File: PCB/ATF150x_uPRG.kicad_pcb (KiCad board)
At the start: 2 copper layers, 38.1 x 22.9 mm, 22 parts, among them J1 Adafruit_2264, J2 Altera JTAG-A+VPP, U2 MAX662A

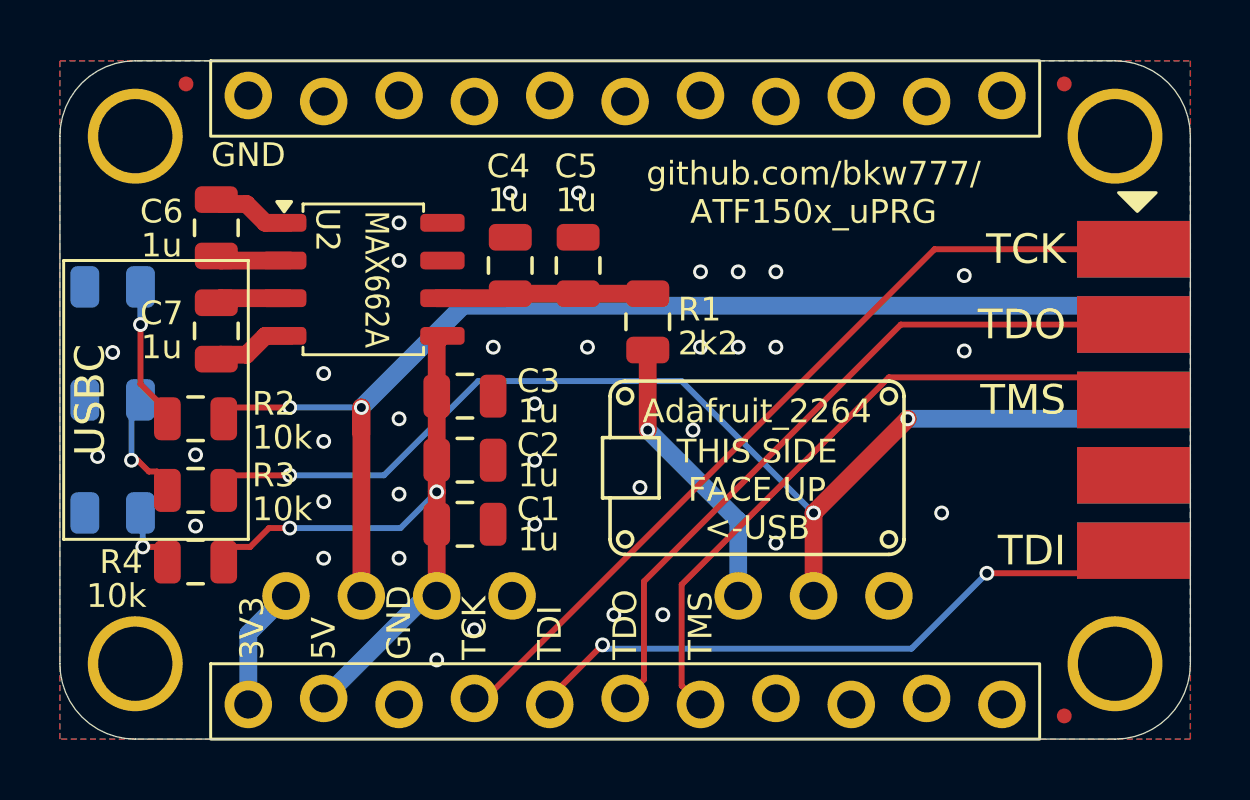
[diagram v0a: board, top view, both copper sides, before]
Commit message: adafruit board use max662 shutdown pin
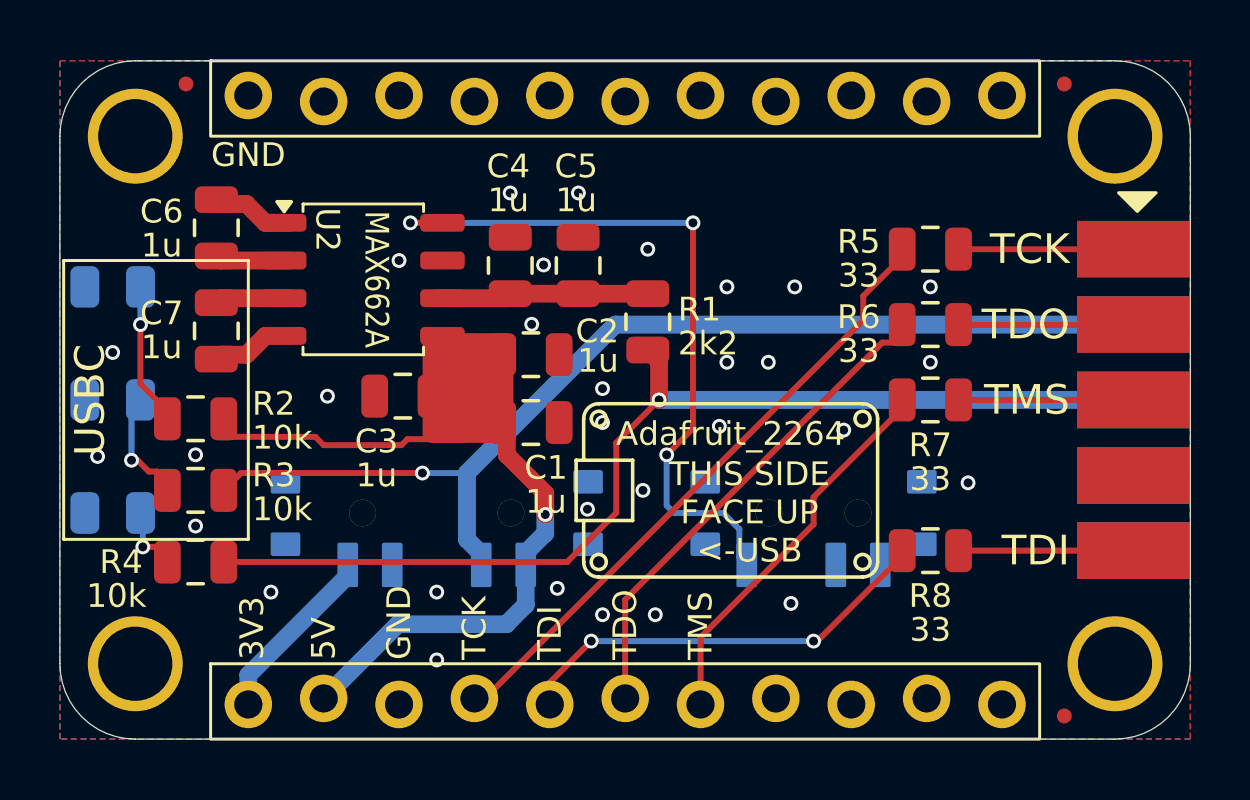
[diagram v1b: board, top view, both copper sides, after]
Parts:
- removed JP1: VCC, 000_LOCAL:PinHeader_1x04_P2.54mm_Horizontal
- removed JP2: VPP, 000_LOCAL:PinHeader_1x03_P2.54mm_Horizontal
- added R5: 33, 000_LOCAL:R_0805, F.Cu at (156.3, 90.2)
- added R6: 33, 000_LOCAL:R_0805, F.Cu at (156.3, 92.7)
- added R7: 33, 000_LOCAL:R_0805, F.Cu at (156.3, 95.2)
- added R8: 33, 000_LOCAL:R_0805, F.Cu at (156.3, 100.3)
- added SW1: VCC, 000_LOCAL:CUS-13B pth, B.Cu at (139.7, 99.1)
- added SW2: VPP, 000_LOCAL:CUS-12B pth, B.Cu at (152.4, 99.1)
- LED1: value VCC -> PWR
- LED2: value VPP -> VCC
- LED3: value PWR -> VPP
- moved C2 4.19 mm to (142.9, 93.7)
- moved C1 4.09 mm to (142.9, 96.0)
- moved C3 2.09 mm to (138.6, 95.1), turned to 180 degrees
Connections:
- J1 pad 4: TCK -> /TCK
- J1 pad 5: TDI -> /TDI
- J1 pad 6: TDO -> /TDO
- J1 pad 7: TMS -> /TMS
- J2 pad 1: TCK -> Net-(J2-TCK)
- J2 pad 3: TDO -> Net-(J2-TDO)
- J2 pad 5: TMS -> Net-(J2-TMS)
- J2 pad 9: TDI -> Net-(J2-TDI)
- R1 pad 1: Net-(JP2-Pad3) -> VPP
- R2 pad 2: VCC -> +5V
- R3 pad 2: VPP -> VCC
- R4 pad 2: +5V -> VPP
- U2 pad 8: GND -> Net-(SW2-A)
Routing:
- net TCK: track 28.5 -> 0.00 mm
- net Net-(SW2-A): track 0.00 -> 24.6 mm, vias 0 -> 3
- net TDO: track 24.3 -> 0.00 mm
- net TMS: track 22.7 -> 0.00 mm
- net TDI: track 22.1 -> 0.00 mm, vias 2 -> 0
- net /TCK: track 0.00 -> 21.3 mm
- net /TDO: track 0.00 -> 16.9 mm
- net /TDI: track 0.00 -> 14.6 mm, vias 0 -> 2
- net /TMS: track 0.00 -> 13.1 mm
- net Net-(JP2-Pad3): track 9.55 -> 0.00 mm, vias 1 -> 0
- net Net-(J2-TMS): track 0.00 -> 5.90 mm
- net Net-(J2-TDO): track 0.00 -> 5.90 mm
- net Net-(J2-TDI): track 0.00 -> 5.90 mm
- net Net-(J2-TCK): track 0.00 -> 5.90 mm
- net +5V: track 22.5 -> 27.5 mm, vias 2 -> 1
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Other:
- board text added: "${COMMENT2}"
- board text added: "${REVISION}"
- board text added: "${TITLE}"
- board text added: "5V TGT 3V3"
- board text added: "OFF 12V"
- board text removed: "12V"
- board text removed: "ATF150x_uPRG"
- board text removed: "BKW JTAG-A+VPP"
- board text removed: "OFF"
- board text removed: "TGT"
- board text removed: "github.com/bkw777/ ATF150x_uPRG"
- board text removed: "v${REVISION}"

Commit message: switch power to max662 instead of using shutdown pin so vpp actually shuts off
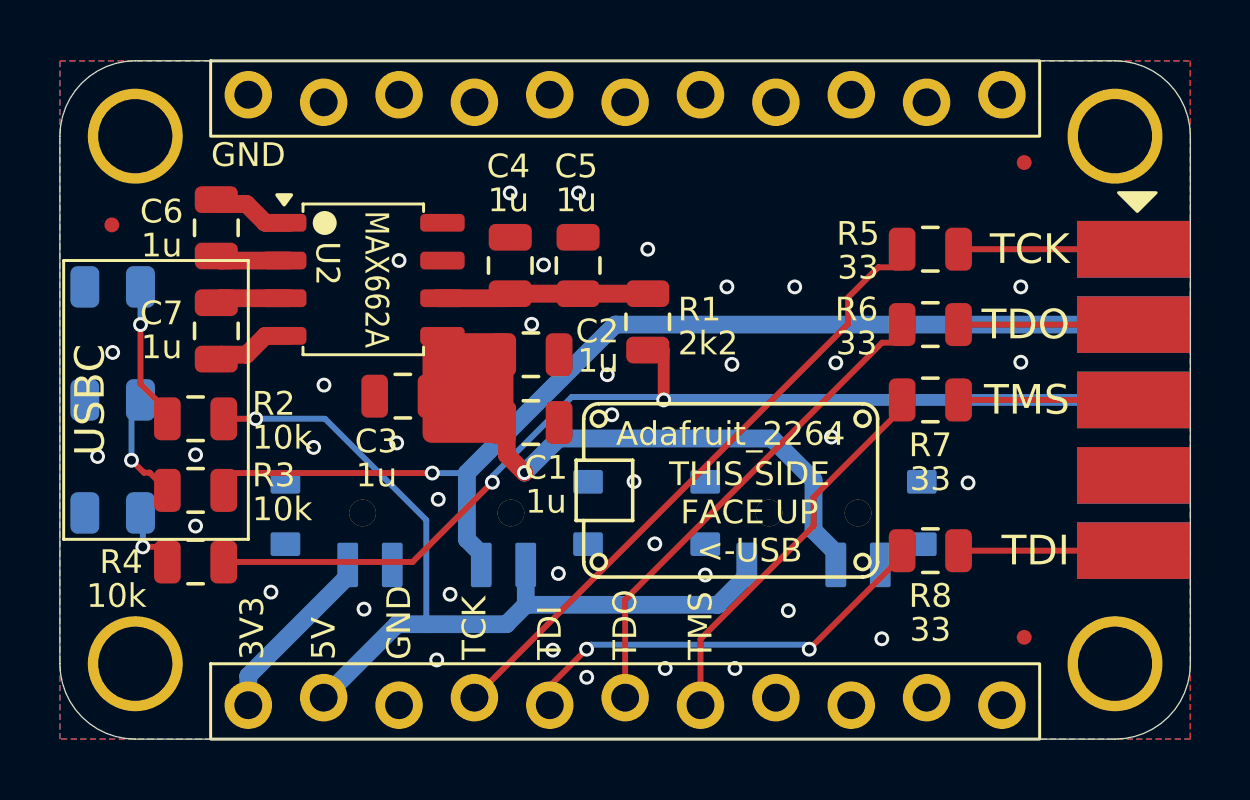
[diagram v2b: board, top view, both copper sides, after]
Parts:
- moved REF** 5.37 mm to (128.8, 89.3)
- moved REF** 2.97 mm to (159.5, 87.2)
- moved REF** 2.97 mm to (159.5, 103.2)
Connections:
- C1 pad 1: +5V -> Net-(SW2-B)
- C2 pad 1: +5V -> Net-(SW2-B)
- C3 pad 1: +5V -> Net-(SW2-B)
- SW2 pad 1: Net-(SW2-A) -> +5V
- SW2 pad 2: GND -> Net-(SW2-B)
- U2 pad 5: +5V -> Net-(SW2-B)
- U2 pad 8: Net-(SW2-A) -> GND
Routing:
- net Net-(SW2-A): track 24.6 -> 0.00 mm, vias 3 -> 0
- net Net-(SW2-B): track 0.00 -> 17.6 mm, vias 0 -> 1
- net +5V: track 27.5 -> 29.4 mm
- net VPP: track 37.0 -> 36.2 mm, vias 1 -> 2
- net GND: vias 31 -> 38

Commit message: fab exports, bom, centroid
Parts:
- added F0: Fiducial_0.5_1.0, 000_LOCAL:Fiducial_0.5_1.0, B.Cu at (159.5, 87.2)
- added F1: Fiducial_0.5_1.0, 000_LOCAL:Fiducial_0.5_1.0, B.Cu at (159.5, 103.2)
- added F2: Fiducial_0.5_1.0, 000_LOCAL:Fiducial_0.5_1.0, B.Cu at (128.8, 89.3)
- LED1: value PWR -> GREEN
- LED2: value VCC -> AMBER
- LED3: value VPP -> RED
- SW1: value VCC -> SP3T
- SW2: value VPP -> SPDT
- moved LED1 0.17 mm to (128.9, 91.4)
- moved LED2 0.17 mm to (128.9, 95.2)
- moved LED3 0.17 mm to (128.9, 99.1)
- renumbered REF** to F3, REF** to F4, REF** to F5, U2 to U1
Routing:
- net VPP: track 36.2 -> 35.6 mm
- net GND: vias 38 -> 33
